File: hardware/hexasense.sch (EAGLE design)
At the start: 11 parts

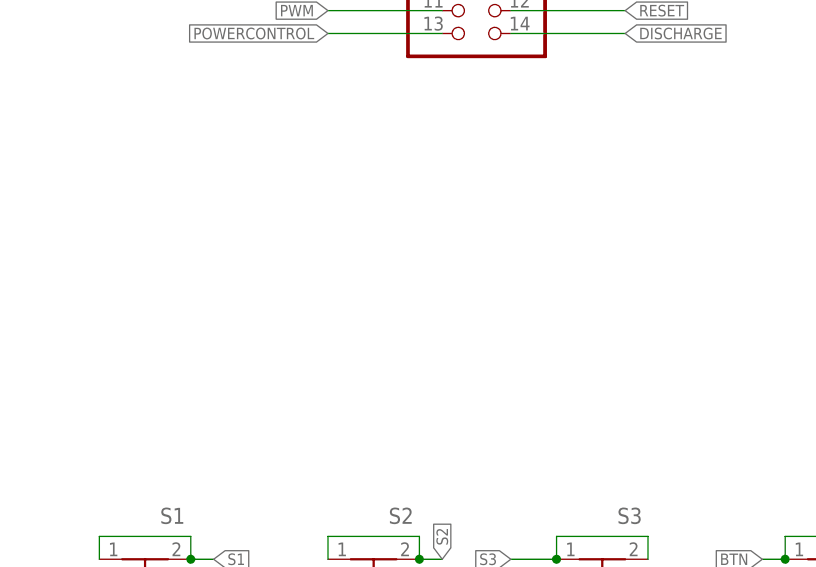
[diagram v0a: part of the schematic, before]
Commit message: added flash chip
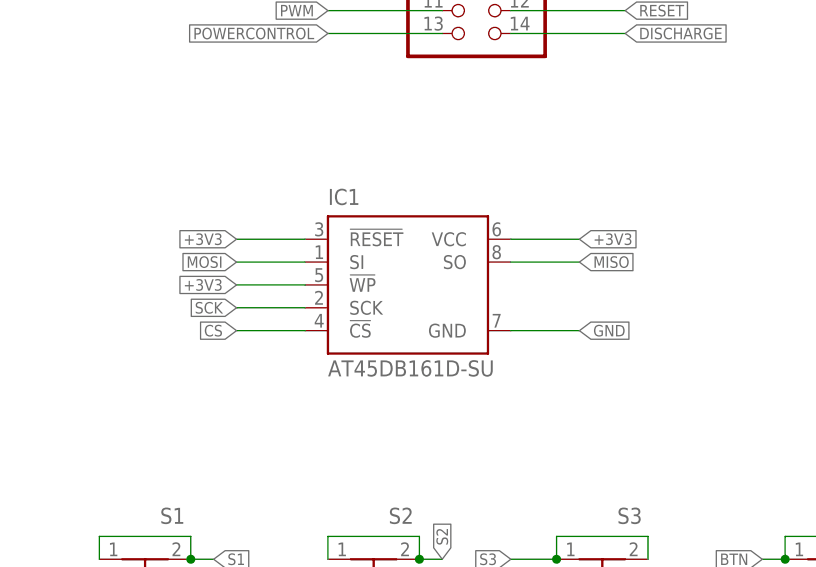
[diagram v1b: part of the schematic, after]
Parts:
- added IC1: AT45DB161D-SU, atmel:AT45DB161D-SU
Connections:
- new net CS: IC1.!CS
- net +3V3: now also IC1.!RESET, IC1.!WP, IC1.VCC
- net GND: now also IC1.GND
- net MISO: now also IC1.SO
- net MOSI: now also IC1.SI
- net SCK: now also IC1.SCK
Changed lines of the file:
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@@
 <part name="C1" library="rcl" deviceset="C-EU" device="C0805" value="100n"/>
 <part name="JP1" library="pinhead" deviceset="PINHD-2X7" device=""/>
+<part name="IC1" library="atmel" deviceset="AT45DB161D" device="-SU"/>
 </parts>
 <sheets>
@@
 <instance part="C1" gate="G$1" x="22.86" y="111.76" rot="R90"/>
 <instance part="JP1" gate="A" x="137.16" y="129.54"/>
+<instance part="IC1" gate="G$1" x="129.54" y="93.98"/>
 </instances>
 <busses>
@@
 <label x="121.92" y="137.16" size="1.27" layer="95" rot="R180" xref="yes"/>
 </segment>
+<segment>
+<pinref part="IC1" gate="G$1" pin="GND"/>
+<wire x1="142.24" y1="88.9" x2="149.86" y2="88.9" width="0.1524" layer="91"/>
+<label x="149.86" y="88.9" size="1.27" layer="95" xref="yes"/>
+</segment>
 </net>
 <net name="+3V3" class="0">
@@
 <label x="154.94" y="137.16" size="1.27" layer="95" xref="yes"/>
 </segment>
+<segment>
+<pinref part="IC1" gate="G$1" pin="VCC"/>
+<wire x1="142.24" y1="99.06" x2="149.86" y2="99.06" width="0.1524" layer="91"/>
+<label x="149.86" y="99.06" size="1.27" layer="95" xref="yes"/>
+</segment>
+<segment>
+<pinref part="IC1" gate="G$1" pin="!RESET"/>
+<wire x1="119.38" y1="99.06" x2="111.76" y2="99.06" width="0.1524" layer="91"/>
+<label x="111.76" y="99.06" size="1.27" layer="95" rot="R180" xref="yes"/>
+</segment>
+<segment>
+<pinref part="IC1" gate="G$1" pin="!WP"/>
+<wire x1="119.38" y1="93.98" x2="111.76" y2="93.98" width="0.1524" layer="91"/>
+<label x="111.76" y="93.98" size="1.27" layer="95" rot="R180" xref="yes"/>
+</segment>
 </net>
 <net name="TEMP_1" class="0">
@@
 <label x="121.92" y="134.62" size="1.27" layer="95" rot="R180" xref="yes"/>
 </segment>
+<segment>
+<pinref part="IC1" gate="G$1" pin="SCK"/>
+<wire x1="119.38" y1="91.44" x2="111.76" y2="91.44" width="0.1524" layer="91"/>
+<label x="111.76" y="91.44" size="1.27" layer="95" rot="R180" xref="yes"/>
+</segment>
 </net>
 <net name="MISO" class="0">
@@
 <label x="121.92" y="132.08" size="1.27" layer="95" rot="R180" xref="yes"/>
 </segment>
+<segment>
+<pinref part="IC1" gate="G$1" pin="SO"/>
+<wire x1="142.24" y1="96.52" x2="149.86" y2="96.52" width="0.1524" layer="91"/>
+<label x="149.86" y="96.52" size="1.27" layer="95" xref="yes"/>
+</segment>
 </net>
 <net name="BUSY" class="0">
@@
 <label x="154.94" y="134.62" size="1.27" layer="95" xref="yes"/>
 </segment>
+<segment>
+<pinref part="IC1" gate="G$1" pin="SI"/>
+<wire x1="119.38" y1="96.52" x2="111.76" y2="96.52" width="0.1524" layer="91"/>
+<label x="111.76" y="96.52" size="1.27" layer="95" rot="R180" xref="yes"/>
+</segment>
 </net>
 <net name="EPD-CSEL" class="0">
@@
 </segment>
 </net>
+<net name="CS" class="0">
+<segment>
+<pinref part="IC1" gate="G$1" pin="!CS"/>
+<wire x1="119.38" y1="88.9" x2="111.76" y2="88.9" width="0.1524" layer="91"/>
+<label x="111.76" y="88.9" size="1.27" layer="95" rot="R180" xref="yes"/>
+</segment>
+</net>

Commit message: now using a real footprint for the epaper display. work in progress
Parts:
- removed JP1: (no value), pinhead:PINHD-2X7
- removed S3: (no value), Ergaenzung:TASTER-9314_SMD
- removed U$8, U$9: HYT271, humidity:HYT271
- added U$2: EPAPER, epaper:EPAPER
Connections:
- net +3V3: now also U$2.VCC; no longer JP1.2, U$8.VDD, U$9.VDD
- net BUSY: now also U$2.UART-RX; no longer JP1.7
- net DISCHARGE: now also U$2.AIN1; no longer JP1.14
- net EPD-CSEL: now also U$2.SPI-SSEL; no longer JP1.6
- net GND: now also U$2.GND; no longer JP1.1, S3.3, S3.4, U$8.GND, U$9.GND
- net MISO: now also U$2.SPI-MISO; no longer JP1.5
- net MOSI: now also U$2.SPI-MOSI; no longer JP1.4
- net POWERCONTROL: now also U$2.AIN0; no longer JP1.13
- net PWM: now also U$2.PWMOUT0; no longer JP1.11
- net RESET: now also U$2.PWMOUT1; no longer JP1.12
- net S3: no longer S3.1, S3.2
- net SCK: now also U$2.SPI-SCK; no longer JP1.3
- net SCL: now also U$2.I2C-SCL; no longer JP1.9, U$8.SCL, U$9.SCL
- net SDA: now also U$2.I2C-SDA; no longer JP1.10, U$8.SDA, U$9.SDA
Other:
- moved on the sheet: IC1
